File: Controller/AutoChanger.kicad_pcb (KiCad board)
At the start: 2 copper layers, 130.1 x 32 mm, 39 parts, among them P1 CONNECT, P10 SENSOR, P11 SENSOR, P12 LOGO, P13 5, P3 1, P4 2, P5 3, P6 4, P7 6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

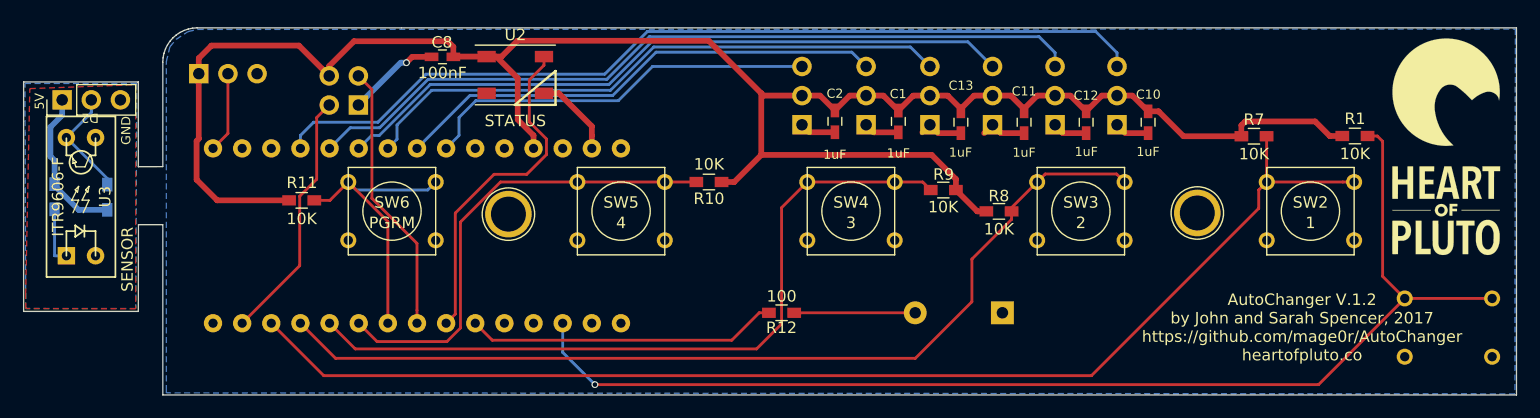
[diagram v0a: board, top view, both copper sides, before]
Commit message: Updated designs across the board
So, lots of small changes as I've tweaked the design.

In order to improve manufacturing, I've changed to 3d printing the main body.
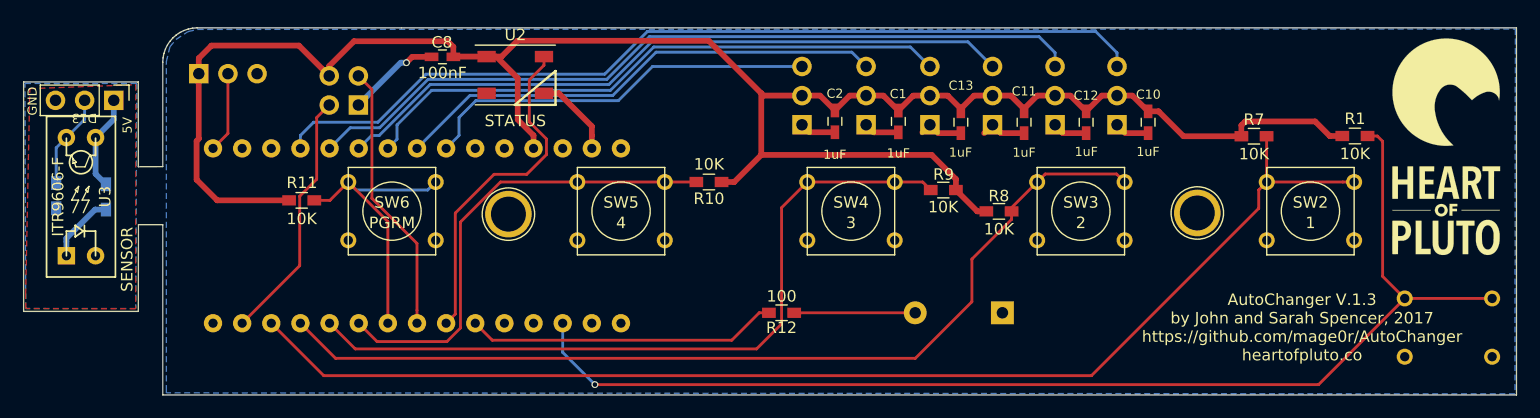
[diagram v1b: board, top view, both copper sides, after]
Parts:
- moved P11 4.50 mm to (84.9, 86.4), turned to 270 degrees
- moved R4 4.48 mm to (84.2, 94.8)
- moved R5 4.45 mm to (79.9, 94.7), turned to 270 degrees
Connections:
- R5 pad 1: +5V -> /D13
- R5 pad 2: /D13 -> GND
- U3 pad 3: /D13 -> +5V
- U3 pad 4: GND -> /D13
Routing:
- net +5V: track 192.0 -> 187.4 mm
- net /D13: track 16.8 -> 15.3 mm
- net Net-(R4-Pad2): track 5.07 -> 6.02 mm
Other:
- board text added: "AutoChanger V.1.3 by John and Sarah Spencer, 2017 https://github.com/mage0r/AutoChanger heartofpluto.co"
- board text added: "D13"
- board text removed: "AutoChanger V.1.2 by John and Sarah Spencer, 2017 https://github.com/mage0r/AutoChanger heartofpluto.co"
- board text removed: "D2"

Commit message: Updated sub board
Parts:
- added R2: 220R, Resistors_SMD:R_0603_HandSoldering, B.Cu at (83.6, 92.7)
- R5: value 10K -> 2M
- moved R4 1.96 mm to (83.6, 96.7)
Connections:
- U3 pad 3: +5V -> Net-(R2-Pad2)
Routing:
- net Net-(R2-Pad2): track 0.00 -> 2.09 mm
- net Net-(R4-Pad2): track 6.02 -> 4.25 mm
- net +5V: track 187.4 -> 188.2 mm
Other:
- outline, holes or cut-outs redrawn
